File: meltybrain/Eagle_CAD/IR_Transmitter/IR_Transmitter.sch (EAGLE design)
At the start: 14 parts, among them J1 AVR_SPI_PROG_3X2NS, Q1 BSS806N, Q2 FDN352AP, U1 LMH6612MAX/NOPB, U2 AP2210K-5.0TRG1

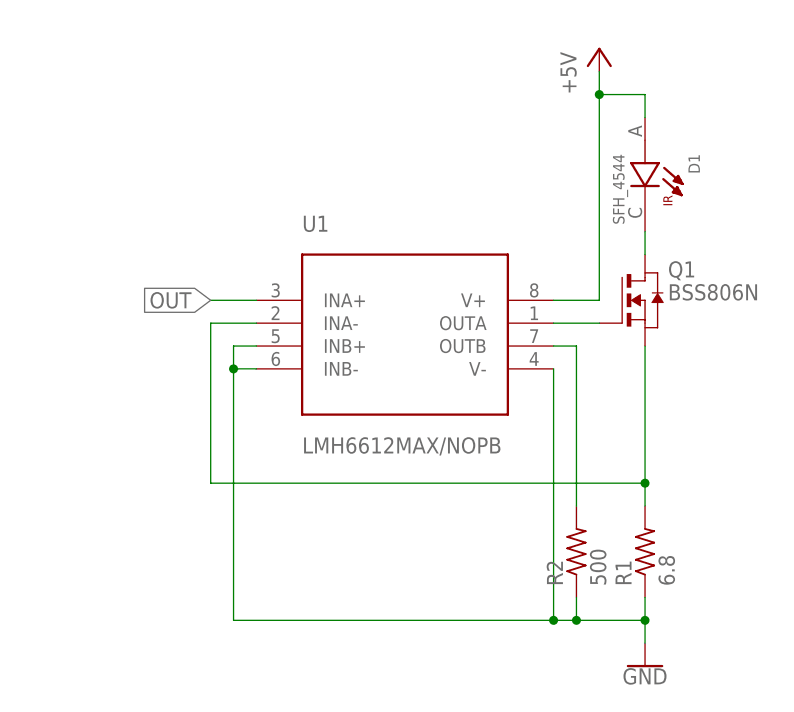
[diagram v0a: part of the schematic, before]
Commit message: Diode Lobes Removed, Board Shrunk
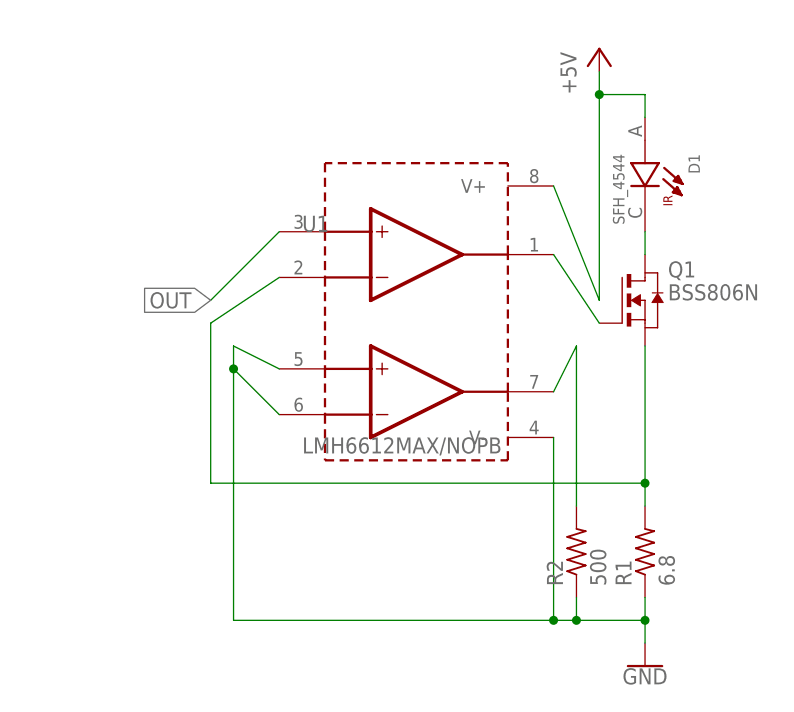
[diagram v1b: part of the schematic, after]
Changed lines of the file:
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@@
 <segment>
 <pinref part="U1" gate="A" pin="INA-"/>
-<wire x1="15.24" y1="0" x2="10.16" y2="0" width="0.1524" layer="91"/>
+<wire x1="17.78" y1="5.08" x2="10.16" y2="0" width="0.1524" layer="91"/>
 <wire x1="10.16" y1="0" x2="10.16" y2="-17.78" width="0.1524" layer="91"/>
 <pinref part="R1" gate="G$1" pin="2"/>
@@
 <pinref part="Q1" gate="G$1" pin="G"/>
 <pinref part="U1" gate="A" pin="OUTA"/>
-<wire x1="53.34" y1="0" x2="48.26" y2="0" width="0.1524" layer="91"/>
+<wire x1="53.34" y1="0" x2="48.26" y2="7.62" width="0.1524" layer="91"/>
 </segment>
 </net>
@@
 <pinref part="U1" gate="A" pin="INB+"/>
 <wire x1="58.42" y1="-33.02" x2="58.42" y2="-35.56" width="0.1524" layer="91"/>
-<wire x1="15.24" y1="-2.54" x2="12.7" y2="-2.54" width="0.1524" layer="91"/>
+<wire x1="17.78" y1="-5.08" x2="12.7" y2="-2.54" width="0.1524" layer="91"/>
 <wire x1="12.7" y1="-2.54" x2="12.7" y2="-5.08" width="0.1524" layer="91"/>
 <pinref part="U1" gate="A" pin="INB-"/>
-<wire x1="12.7" y1="-5.08" x2="15.24" y2="-5.08" width="0.1524" layer="91"/>
+<wire x1="12.7" y1="-5.08" x2="17.78" y2="-10.16" width="0.1524" layer="91"/>
 <wire x1="12.7" y1="-5.08" x2="12.7" y2="-33.02" width="0.1524" layer="91"/>
 <wire x1="12.7" y1="-33.02" x2="48.26" y2="-33.02" width="0.1524" layer="91"/>
@@
 <junction x="50.8" y="-33.02"/>
 <pinref part="U1" gate="A" pin="V-"/>
-<wire x1="48.26" y1="-5.08" x2="48.26" y2="-33.02" width="0.1524" layer="91"/>
+<wire x1="48.26" y1="-12.7" x2="48.26" y2="-33.02" width="0.1524" layer="91"/>
 <junction x="48.26" y="-33.02"/>
 </segment>
@@
 <pinref part="U1" gate="A" pin="OUTB"/>
 <wire x1="50.8" y1="-20.32" x2="50.8" y2="-2.54" width="0.1524" layer="91"/>
-<wire x1="50.8" y1="-2.54" x2="48.26" y2="-2.54" width="0.1524" layer="91"/>
+<wire x1="50.8" y1="-2.54" x2="48.26" y2="-7.62" width="0.1524" layer="91"/>
 </segment>
 </net>
@@
 <pinref part="U1" gate="A" pin="V+"/>
 <pinref part="P+1" gate="1" pin="+5V"/>
-<wire x1="48.26" y1="2.54" x2="53.34" y2="2.54" width="0.1524" layer="91"/>
+<wire x1="48.26" y1="15.24" x2="53.34" y2="2.54" width="0.1524" layer="91"/>
 <wire x1="53.34" y1="2.54" x2="53.34" y2="25.4" width="0.1524" layer="91"/>
 <pinref part="D1" gate="G$1" pin="A"/>
@@
 <segment>
 <pinref part="U1" gate="A" pin="INA+"/>
-<wire x1="15.24" y1="2.54" x2="10.16" y2="2.54" width="0.1524" layer="91"/>
+<wire x1="17.78" y1="10.16" x2="10.16" y2="2.54" width="0.1524" layer="91"/>
 <label x="10.16" y="2.54" size="1.778" layer="95" rot="R180" xref="yes"/>
 </segment>
